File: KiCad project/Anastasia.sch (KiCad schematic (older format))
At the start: 0 parts

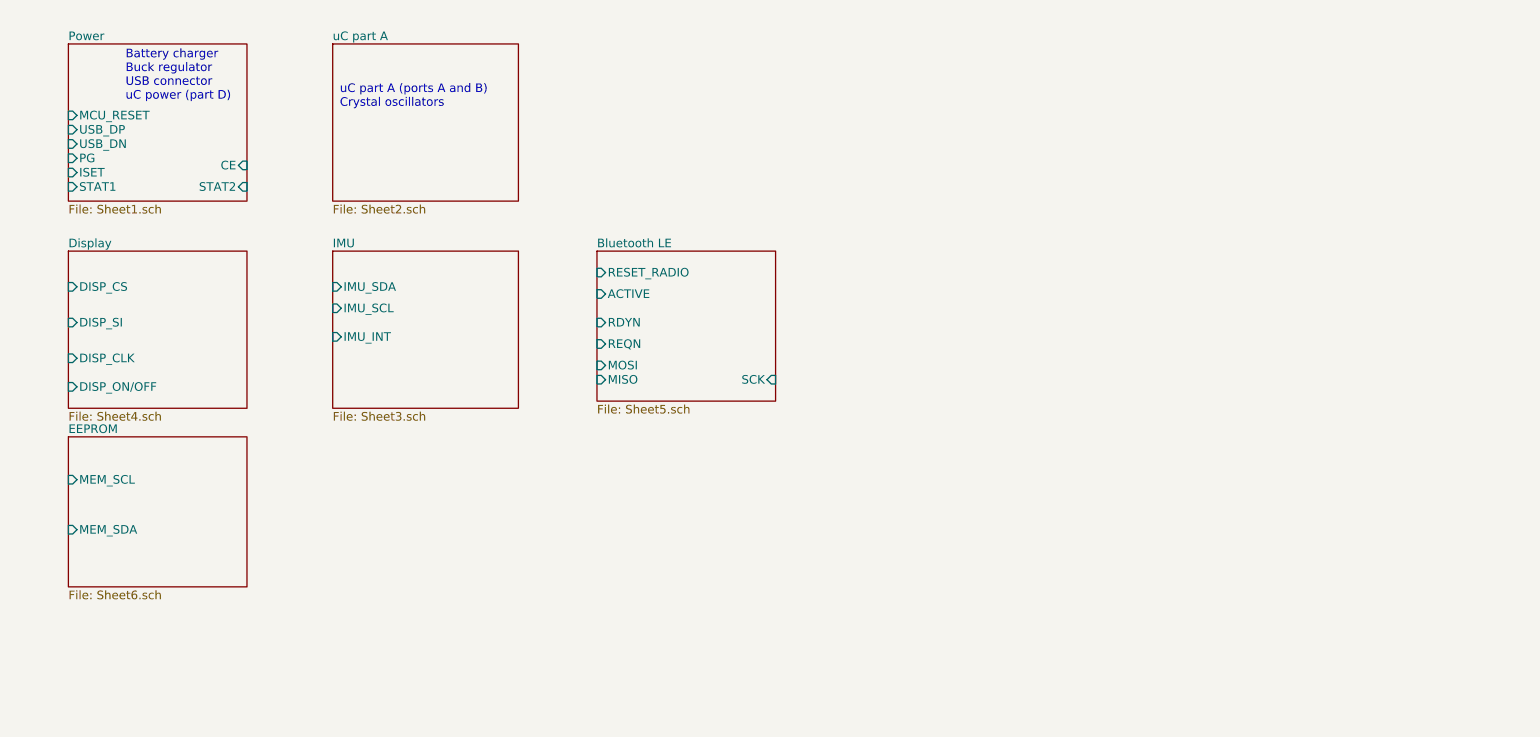
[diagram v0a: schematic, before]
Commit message: IC packages, bugfixes
drawings for IC packages, associations, schematic fixes
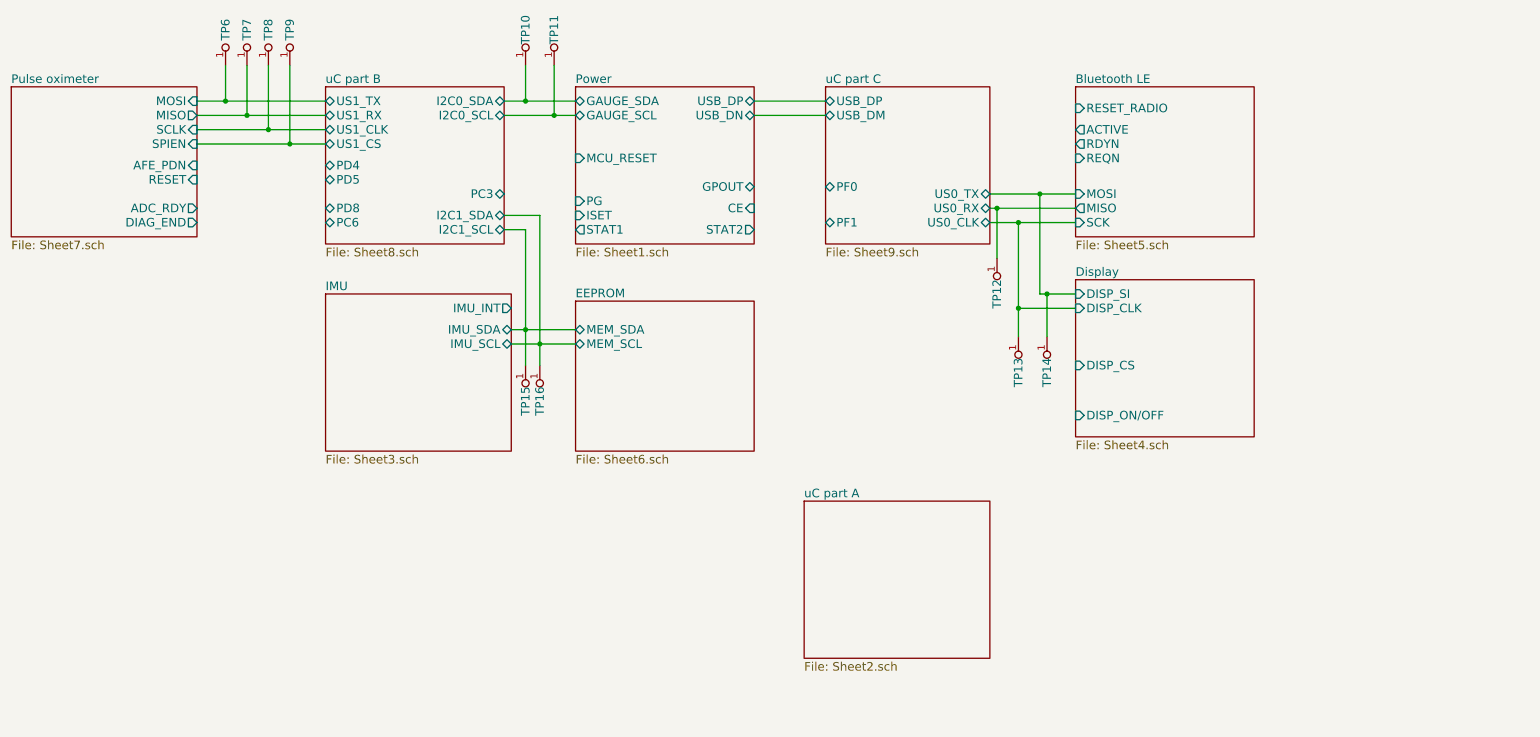
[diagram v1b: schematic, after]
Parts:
- added TP10, TP11, TP12, TP13, TP14, TP15, TP16, TP6, TP7, TP8, TP9: TESTPAD, symbol TESTPAD
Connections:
- net Bluetooth LE/MISO: now also TP12.1
- net Bluetooth LE/MOSI: now also TP14.1
- net Bluetooth LE/SCK: now also TP13.1
- net EEPROM/MEM_SCL: now also TP16.1
- net EEPROM/MEM_SDA: now also TP15.1
- new net Power/GAUGE_SCL: TP11.1
- new net Power/GAUGE_SDA: TP10.1
- new net Pulse oximeter /MISO: TP7.1
- new net Pulse oximeter /MOSI: TP6.1
- new net Pulse oximeter /SCLK: TP8.1
- new net Pulse oximeter /SPIEN: TP9.1
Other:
- note removed: "Battery charger\nBuck regulator\nUSB connector\nuC power (part D)"
- note removed: "uC part A (ports A and B)\nCrystal oscillators\n"

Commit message: New packages, PCB
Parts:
- TP1: renamed from TP6; footprint (none) -> Measurement_Points:Measurement_Point_Round-SMD-Pad_Small
- TP10: renamed from TP15; footprint (none) -> Measurement_Points:Measurement_Point_Round-SMD-Pad_Small
- TP11: renamed from TP16; footprint (none) -> Measurement_Points:Measurement_Point_Round-SMD-Pad_Small
- TP2: renamed from TP7; footprint (none) -> Measurement_Points:Measurement_Point_Round-SMD-Pad_Small
- TP3: renamed from TP8; footprint (none) -> Measurement_Points:Measurement_Point_Round-SMD-Pad_Small
- TP4: renamed from TP9; footprint (none) -> Measurement_Points:Measurement_Point_Round-SMD-Pad_Small
- TP5: renamed from TP10; footprint (none) -> Measurement_Points:Measurement_Point_Round-SMD-Pad_Small
- TP6: renamed from TP11; footprint (none) -> Measurement_Points:Measurement_Point_Round-SMD-Pad_Small
- TP7: renamed from TP12; footprint (none) -> Measurement_Points:Measurement_Point_Round-SMD-Pad_Small
- TP8: renamed from TP13; footprint (none) -> Measurement_Points:Measurement_Point_Round-SMD-Pad_Small
- TP9: renamed from TP14; footprint (none) -> Measurement_Points:Measurement_Point_Round-SMD-Pad_Small
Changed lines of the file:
@@
 Connection ~ 4400 2950
 $Comp
-L TESTPAD TP6
+L TESTPAD TP1
 U 1 1 550D1F0B
 P 2200 1000
-F 0 "TP6" H 2450 1000 60  0000 C CNN
+F 0 "TP1" H 2450 1000 60  0000 C CNN
 F 1 "TESTPAD" H 2250 800 60  0001 C CNN
-F 2 "" H 2450 1000 60  0000 C CNN
+F 2 "Measurement_Points:Measurement_Point_Round-SMD-Pad_Small" H 2450 1000 60  0001 C CNN
 F 3 "" H 2450 1000 60  0000 C CNN
 	1    2200 1000
@@
 $EndComp
 $Comp
-L TESTPAD TP7
+L TESTPAD TP2
 U 1 1 550D1F40
 P 2350 1000
-F 0 "TP7" H 2600 1000 60  0000 C CNN
+F 0 "TP2" H 2600 1000 60  0000 C CNN
 F 1 "TESTPAD" H 2400 800 60  0001 C CNN
-F 2 "" H 2600 1000 60  0000 C CNN
+F 2 "Measurement_Points:Measurement_Point_Round-SMD-Pad_Small" H 2600 1000 60  0001 C CNN
 F 3 "" H 2600 1000 60  0000 C CNN
 	1    2350 1000
@@
 $EndComp
 $Comp
-L TESTPAD TP8
+L TESTPAD TP3
 U 1 1 550D1F5F
 P 2500 1000
-F 0 "TP8" H 2750 1000 60  0000 C CNN
+F 0 "TP3" H 2750 1000 60  0000 C CNN
 F 1 "TESTPAD" H 2550 800 60  0001 C CNN
-F 2 "" H 2750 1000 60  0000 C CNN
+F 2 "Measurement_Points:Measurement_Point_Round-SMD-Pad_Small" H 2750 1000 60  0001 C CNN
 F 3 "" H 2750 1000 60  0000 C CNN
 	1    2500 1000
@@
 $EndComp
 $Comp
-L TESTPAD TP9
+L TESTPAD TP4
 U 1 1 550D1F7E
 P 2650 1000
-F 0 "TP9" H 2900 1000 60  0000 C CNN
+F 0 "TP4" H 2900 1000 60  0000 C CNN
 F 1 "TESTPAD" H 2700 800 60  0001 C CNN
-F 2 "" H 2900 1000 60  0000 C CNN
+F 2 "Measurement_Points:Measurement_Point_Round-SMD-Pad_Small" H 2900 1000 60  0001 C CNN
 F 3 "" H 2900 1000 60  0000 C CNN
 	1    2650 1000
@@
 Connection ~ 2650 1550
 $Comp
-L TESTPAD TP10
+L TESTPAD TP5
 U 1 1 550D353F
 P 4300 1000
-F 0 "TP10" H 4550 1000 60  0000 C CNN
+F 0 "TP5" H 4550 1000 60  0000 C CNN
 F 1 "TESTPAD" H 4350 800 60  0001 C CNN
-F 2 "" H 4550 1000 60  0000 C CNN
+F 2 "Measurement_Points:Measurement_Point_Round-SMD-Pad_Small" H 4550 1000 60  0001 C CNN
 F 3 "" H 4550 1000 60  0000 C CNN
 	1    4300 1000
@@
 $EndComp
 $Comp
-L TESTPAD TP11
+L TESTPAD TP6
 U 1 1 550D3564
 P 4500 1000
-F 0 "TP11" H 4750 1000 60  0000 C CNN
+F 0 "TP6" H 4750 1000 60  0000 C CNN
 F 1 "TESTPAD" H 4550 800 60  0001 C CNN
-F 2 "" H 4750 1000 60  0000 C CNN
+F 2 "Measurement_Points:Measurement_Point_Round-SMD-Pad_Small" H 4750 1000 60  0001 C CNN
 F 3 "" H 4750 1000 60  0000 C CNN
 	1    4500 1000
@@
 $EndComp
 $Comp
-L TESTPAD TP15
+L TESTPAD TP10
 U 1 1 550D3583
 P 4300 3100
-F 0 "TP15" H 4550 3100 60  0000 C CNN
+F 0 "TP10" H 4550 3100 60  0000 C CNN
 F 1 "TESTPAD" H 4350 2900 60  0001 C CNN
-F 2 "" H 4550 3100 60  0000 C CNN
+F 2 "Measurement_Points:Measurement_Point_Round-SMD-Pad_Small" H 4550 3100 60  0001 C CNN
 F 3 "" H 4550 3100 60  0000 C CNN
 	1    4300 3100
@@
 $EndComp
 $Comp
-L TESTPAD TP16
+L TESTPAD TP11
 U 1 1 550D359E
 P 4400 3100
-F 0 "TP16" H 4650 3100 60  0000 C CNN
+F 0 "TP11" H 4650 3100 60  0000 C CNN
 F 1 "TESTPAD" H 4450 2900 60  0001 C CNN
-F 2 "" H 4650 3100 60  0000 C CNN
+F 2 "Measurement_Points:Measurement_Point_Round-SMD-Pad_Small" H 4650 3100 60  0001 C CNN
 F 3 "" H 4650 3100 60  0000 C CNN
 	1    4400 3100
@@
 Connection ~ 4500 1350
 $Comp
-L TESTPAD TP13
+L TESTPAD TP8
 U 1 1 550D3905
 P 7750 2900
-F 0 "TP13" H 8000 2900 60  0000 C CNN
+F 0 "TP8" H 8000 2900 60  0000 C CNN
 F 1 "TESTPAD" H 7800 2700 60  0001 C CNN
-F 2 "" H 8000 2900 60  0000 C CNN
+F 2 "Measurement_Points:Measurement_Point_Round-SMD-Pad_Small" H 8000 2900 60  0001 C CNN
 F 3 "" H 8000 2900 60  0000 C CNN
 	1    7750 2900
@@
 $EndComp
 $Comp
-L TESTPAD TP14
+L TESTPAD TP9
 U 1 1 550D3920
 P 7950 2900
-F 0 "TP14" H 8200 2900 60  0000 C CNN
+F 0 "TP9" H 8200 2900 60  0000 C CNN
 F 1 "TESTPAD" H 8000 2700 60  0001 C CNN
-F 2 "" H 8200 2900 60  0000 C CNN
+F 2 "Measurement_Points:Measurement_Point_Round-SMD-Pad_Small" H 8200 2900 60  0001 C CNN
 F 3 "" H 8200 2900 60  0000 C CNN
 	1    7950 2900
@@
 Connection ~ 7950 2600
 $Comp
-L TESTPAD TP12
+L TESTPAD TP7
 U 1 1 550D3AEA
 P 7600 2350
-F 0 "TP12" H 7850 2350 60  0000 C CNN
+F 0 "TP7" H 7850 2350 60  0000 C CNN
 F 1 "TESTPAD" H 7650 2150 60  0001 C CNN
-F 2 "" H 7850 2350 60  0000 C CNN
+F 2 "Measurement_Points:Measurement_Point_Round-SMD-Pad_Small" H 7850 2350 60  0001 C CNN
 F 3 "" H 7850 2350 60  0000 C CNN
 	1    7600 2350

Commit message: Schematics, PCB design
New schematics for the pulse oximeter, PCB layout design
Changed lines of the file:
@@
 $EndSheet
 $Sheet
-S 6250 4050 1300 1100
+S 2900 3900 1300 1100
 U 5504D17E
 F0 "uC part A" 60
 F1 "Sheet2.sch" 60
+F2 "PA8" I L 2900 4100 60
 $EndSheet
 $Sheet
@@
 F2 "IMU_SDA" B R 4200 2850 60
 F3 "IMU_SCL" B R 4200 2950 60
-F4 "IMU_INT" O R 4200 2700 60
+F4 "IMU_INT" O L 2900 3550 60
 $EndSheet
 $Sheet
@@
 	7600 2350 7600 2000
 Connection ~ 7600 2000
+Wire Wire Line
+	2900 4100 2650 4100
+Wire Wire Line
+	2650 4100 2650 3550
+Wire Wire Line
+	2650 3550 2900 3550
 $EndSCHEMATC

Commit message: PCB design
Routing for the main components, except for the power section
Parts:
- TP1, TP10, TP11, TP2, TP3, TP4, TP5, TP6, TP7, TP8, TP9: footprint Measurement_Points:Measurement_Point_Round-SMD-Pad_Small -> Anastasia:Test_Point_Round-SMD-Pad
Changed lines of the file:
@@
 F1 "Sheet2.sch" 60
 F2 "PA8" I L 2900 4100 60
+F3 "PA0" T R 4200 4100 60
 $EndSheet
 $Sheet
@@
 F5 "SPIEN" I R 2000 1550 60
 F6 "RESET" I R 2000 1800 60
-F7 "ADC_RDY" O R 2000 2000 60
-F8 "AFE_PDN" I R 2000 1700 60
+F7 "ADC_RDY" O R 2000 1700 60
+F8 "AFE_PDN" I R 2000 2000 60
 F9 "DIAG_END" O R 2000 2100 60
 $EndSheet
@@
 F11 "PD5" T L 2900 1800 60
 F12 "PC3" T R 4150 1900 60
-F13 "PD8" T L 2900 2000 60
-F14 "PC6" T L 2900 2100 60
+F13 "PD8" T R 4150 1600 60
+F14 "PC6" T R 4150 1750 60
+F15 "PD6" B L 2900 2100 60
+F16 "PD7" B L 2900 2000 60
 $EndSheet
 $Sheet
@@
 F5 "US0_RX" T R 7550 2000 60
 F6 "US0_CLK" T R 7550 2100 60
-F7 "PF0" T L 6400 1850 60
-F8 "PF1" T L 6400 2100 60
+F7 "PF0" T R 7550 1300 60
+F8 "PF1" T R 7550 1550 60
+F9 "PF2" T R 7550 1650 60
 $EndSheet
 $Sheet
@@
 F 0 "TP1" H 2450 1000 60  0000 C CNN
 F 1 "TESTPAD" H 2250 800 60  0001 C CNN
-F 2 "Measurement_Points:Measurement_Point_Round-SMD-Pad_Small" H 2450 1000 60  0001 C CNN
+F 2 "Anastasia:Test_Point_Round-SMD-Pad" H 2450 1000 60  0001 C CNN
 F 3 "" H 2450 1000 60  0000 C CNN
 	1    2200 1000
@@
 F 0 "TP2" H 2600 1000 60  0000 C CNN
 F 1 "TESTPAD" H 2400 800 60  0001 C CNN
-F 2 "Measurement_Points:Measurement_Point_Round-SMD-Pad_Small" H 2600 1000 60  0001 C CNN
+F 2 "Anastasia:Test_Point_Round-SMD-Pad" H 2600 1000 60  0001 C CNN
 F 3 "" H 2600 1000 60  0000 C CNN
 	1    2350 1000
@@
 F 0 "TP3" H 2750 1000 60  0000 C CNN
 F 1 "TESTPAD" H 2550 800 60  0001 C CNN
-F 2 "Measurement_Points:Measurement_Point_Round-SMD-Pad_Small" H 2750 1000 60  0001 C CNN
+F 2 "Anastasia:Test_Point_Round-SMD-Pad" H 2750 1000 60  0001 C CNN
 F 3 "" H 2750 1000 60  0000 C CNN
 	1    2500 1000
@@
 F 0 "TP4" H 2900 1000 60  0000 C CNN
 F 1 "TESTPAD" H 2700 800 60  0001 C CNN
-F 2 "Measurement_Points:Measurement_Point_Round-SMD-Pad_Small" H 2900 1000 60  0001 C CNN
+F 2 "Anastasia:Test_Point_Round-SMD-Pad" H 2900 1000 60  0001 C CNN
 F 3 "" H 2900 1000 60  0000 C CNN
 	1    2650 1000
@@
 F 0 "TP5" H 4550 1000 60  0000 C CNN
 F 1 "TESTPAD" H 4350 800 60  0001 C CNN
-F 2 "Measurement_Points:Measurement_Point_Round-SMD-Pad_Small" H 4550 1000 60  0001 C CNN
+F 2 "Anastasia:Test_Point_Round-SMD-Pad" H 4550 1000 60  0001 C CNN
 F 3 "" H 4550 1000 60  0000 C CNN
 	1    4300 1000
@@
 F 0 "TP6" H 4750 1000 60  0000 C CNN
 F 1 "TESTPAD" H 4550 800 60  0001 C CNN
-F 2 "Measurement_Points:Measurement_Point_Round-SMD-Pad_Small" H 4750 1000 60  0001 C CNN
+F 2 "Anastasia:Test_Point_Round-SMD-Pad" H 4750 1000 60  0001 C CNN
 F 3 "" H 4750 1000 60  0000 C CNN
 	1    4500 1000
@@
 F 0 "TP10" H 4550 3100 60  0000 C CNN
 F 1 "TESTPAD" H 4350 2900 60  0001 C CNN
-F 2 "Measurement_Points:Measurement_Point_Round-SMD-Pad_Small" H 4550 3100 60  0001 C CNN
+F 2 "Anastasia:Test_Point_Round-SMD-Pad" H 4550 3100 60  0001 C CNN
 F 3 "" H 4550 3100 60  0000 C CNN
 	1    4300 3100
@@
 F 0 "TP11" H 4650 3100 60  0000 C CNN
 F 1 "TESTPAD" H 4450 2900 60  0001 C CNN
-F 2 "Measurement_Points:Measurement_Point_Round-SMD-Pad_Small" H 4650 3100 60  0001 C CNN
+F 2 "Anastasia:Test_Point_Round-SMD-Pad" H 4650 3100 60  0001 C CNN
 F 3 "" H 4650 3100 60  0000 C CNN
 	1    4400 3100
@@
 F 0 "TP8" H 8000 2900 60  0000 C CNN
 F 1 "TESTPAD" H 7800 2700 60  0001 C CNN
-F 2 "Measurement_Points:Measurement_Point_Round-SMD-Pad_Small" H 8000 2900 60  0001 C CNN
+F 2 "Anastasia:Test_Point_Round-SMD-Pad" H 8000 2900 60  0001 C CNN
 F 3 "" H 8000 2900 60  0000 C CNN
 	1    7750 2900
@@
 F 0 "TP9" H 8200 2900 60  0000 C CNN
 F 1 "TESTPAD" H 8000 2700 60  0001 C CNN
-F 2 "Measurement_Points:Measurement_Point_Round-SMD-Pad_Small" H 8200 2900 60  0001 C CNN
+F 2 "Anastasia:Test_Point_Round-SMD-Pad" H 8200 2900 60  0001 C CNN
 F 3 "" H 8200 2900 60  0000 C CNN
 	1    7950 2900
@@
 F 0 "TP7" H 7850 2350 60  0000 C CNN
 F 1 "TESTPAD" H 7650 2150 60  0001 C CNN
-F 2 "Measurement_Points:Measurement_Point_Round-SMD-Pad_Small" H 7850 2350 60  0001 C CNN
+F 2 "Anastasia:Test_Point_Round-SMD-Pad" H 7850 2350 60  0001 C CNN
 F 3 "" H 7850 2350 60  0000 C CNN
 	1    7600 2350
@@
 Wire Wire Line
 	2650 3550 2900 3550
+Wire Wire Line
+	8150 1650 7550 1650
+Wire Wire Line
+	8150 1450 7950 1450
+Wire Wire Line
+	7950 1450 7950 850
+Wire Wire Line
+	7950 850  9700 850
+Wire Wire Line
+	9700 850  9700 4100
+Wire Wire Line
+	9700 4100 4200 4100
+Wire Wire Line
+	8150 1300 7550 1300
+Wire Wire Line
+	7550 1550 8150 1550
+Connection ~ 5100 1450
+Wire Wire Line
+	2900 1700 2000 1700
+Wire Wire Line
+	2000 1800 2900 1800
+Wire Wire Line
+	2000 2000 2900 2000
+Wire Wire Line
+	2000 2100 2900 2100
 $EndSCHEMATC

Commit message: PCB finalised, Gerbers created for v0.5
New footprints, fixes in schematic, PCB final design, plotted Gerbers
for prototype production
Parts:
- removed TP1, TP10, TP2, TP3, TP4, TP5, TP6, TP8, TP9: TESTPAD, Anastasia:Test_Point_Round-SMD-Pad, symbol TESTPAD
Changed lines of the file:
@@
 $EndDescr
-$Sheet
-S 4650 1150 1250 1100
-U 55046F13
-F0 "Power" 60
-F1 "Sheet1.sch" 60
-F2 "MCU_RESET" I L 4650 1650 60
-F3 "USB_DP" T R 5900 1250 60
-F4 "USB_DN" T R 5900 1350 60
-F5 "PG" I L 4650 1950 60
-F6 "ISET" I L 4650 2050 60
-F7 "STAT1" O L 4650 2150 60
-F8 "STAT2" O R 5900 2150 60
-F9 "CE" I R 5900 2000 60
-F10 "GPOUT" B R 5900 1850 60
-F11 "GAUGE_SCL" B L 4650 1350 60
-F12 "GAUGE_SDA" B L 4650 1250 60
-$EndSheet
 $Sheet
 S 2900 3900 1300 1100
@@
 F2 "PA8" I L 2900 4100 60
 F3 "PA0" T R 4200 4100 60
+F4 "PA1" T R 4200 4250 60
+F5 "PA2" T R 4200 4400 60
+F6 "PA9" T R 4200 4850 60
+F7 "PA10" T R 4200 4700 60
 $EndSheet
 $Sheet
@@
 F0 "Display" 60
 F1 "Sheet4.sch" 60
-F2 "DISP_CS" I L 8150 3100 60
+F2 "DISP_CS" I L 8150 3300 60
 F3 "DISP_SI" I L 8150 2600 60
 F4 "DISP_CLK" I L 8150 2700 60
@@
 F8 "PF1" T R 7550 1550 60
 F9 "PF2" T R 7550 1650 60
+F10 "PE9" T L 6400 2150 60
+F11 "PE8" T L 6400 2000 60
 $EndSheet
 $Sheet
@@
 	4150 1250 4650 1250
 Wire Wire Line
-	4650 1350 4150 1350
+	4150 1350 4650 1350
 Wire Wire Line
 	2000 1250 2900 1250
@@
 Connection ~ 7900 1900
 Wire Wire Line
-	7750 2100 7750 2900
-Wire Wire Line
 	7750 2700 8150 2700
 Connection ~ 7750 2100
@@
 	4200 2950 4650 2950
 Wire Wire Line
-	4150 2150 4300 2150
-Wire Wire Line
-	4300 2150 4300 3100
-Connection ~ 4300 2850
-Wire Wire Line
-	4150 2050 4400 2050
-Wire Wire Line
-	4400 2050 4400 3100
+	4400 2950 4400 3100
 Connection ~ 4400 2950
-$Comp
-L TESTPAD TP1
-U 1 1 550D1F0B
-P 2200 1000
-F 0 "TP1" H 2450 1000 60  0000 C CNN
-F 1 "TESTPAD" H 2250 800 60  0001 C CNN
-F 2 "Anastasia:Test_Point_Round-SMD-Pad" H 2450 1000 60  0001 C CNN
-F 3 "" H 2450 1000 60  0000 C CNN
-	1    2200 1000
-	0    -1   -1   0
-$EndComp
-$Comp
-L TESTPAD TP2
-U 1 1 550D1F40
-P 2350 1000
-F 0 "TP2" H 2600 1000 60  0000 C CNN
-F 1 "TESTPAD" H 2400 800 60  0001 C CNN
-F 2 "Anastasia:Test_Point_Round-SMD-Pad" H 2600 1000 60  0001 C CNN
-F 3 "" H 2600 1000 60  0000 C CNN
-	1    2350 1000
-	0    -1   -1   0
-$EndComp
-$Comp
-L TESTPAD TP3
-U 1 1 550D1F5F
-P 2500 1000
-F 0 "TP3" H 2750 1000 60  0000 C CNN
-F 1 "TESTPAD" H 2550 800 60  0001 C CNN
-F 2 "Anastasia:Test_Point_Round-SMD-Pad" H 2750 1000 60  0001 C CNN
-F 3 "" H 2750 1000 60  0000 C CNN
-	1    2500 1000
-	0    -1   -1   0
-$EndComp
-$Comp
-L TESTPAD TP4
-U 1 1 550D1F7E
-P 2650 1000
-F 0 "TP4" H 2900 1000 60  0000 C CNN
-F 1 "TESTPAD" H 2700 800 60  0001 C CNN
-F 2 "Anastasia:Test_Point_Round-SMD-Pad" H 2900 1000 60  0001 C CNN
-F 3 "" H 2900 1000 60  0000 C CNN
-	1    2650 1000
-	0    -1   -1   0
-$EndComp
-Wire Wire Line
-	2200 1000 2200 1250
-Connection ~ 2200 1250
-Wire Wire Line
-	2350 1000 2350 1350
-Connection ~ 2350 1350
-Wire Wire Line
-	2500 1000 2500 1450
-Connection ~ 2500 1450
-Wire Wire Line
-	2650 1000 2650 1550
-Connection ~ 2650 1550
-$Comp
-L TESTPAD TP5
-U 1 1 550D353F
-P 4300 1000
-F 0 "TP5" H 4550 1000 60  0000 C CNN
-F 1 "TESTPAD" H 4350 800 60  0001 C CNN
-F 2 "Anastasia:Test_Point_Round-SMD-Pad" H 4550 1000 60  0001 C CNN
-F 3 "" H 4550 1000 60  0000 C CNN
-	1    4300 1000
-	0    -1   -1   0
-$EndComp
-$Comp
-L TESTPAD TP6
-U 1 1 550D3564
-P 4500 1000
-F 0 "TP6" H 4750 1000 60  0000 C CNN
-F 1 "TESTPAD" H 4550 800 60  0001 C CNN
-F 2 "Anastasia:Test_Point_Round-SMD-Pad" H 4750 1000 60  0001 C CNN
-F 3 "" H 4750 1000 60  0000 C CNN
-	1    4500 1000
-	0    -1   -1   0
-$EndComp
-$Comp
-L TESTPAD TP10
-U 1 1 550D3583
-P 4300 3100
-F 0 "TP10" H 4550 3100 60  0000 C CNN
-F 1 "TESTPAD" H 4350 2900 60  0001 C CNN
-F 2 "Anastasia:Test_Point_Round-SMD-Pad" H 4550 3100 60  0001 C CNN
-F 3 "" H 4550 3100 60  0000 C CNN
-	1    4300 3100
-	0    1    1    0
-$EndComp
 $Comp
 L TESTPAD TP11
@@
 	0    1    1    0
 $EndComp
-Wire Wire Line
-	4300 1000 4300 1250
-Connection ~ 4300 1250
-Wire Wire Line
-	4500 1000 4500 1350
-Connection ~ 4500 1350
-$Comp
-L TESTPAD TP8
-U 1 1 550D3905
-P 7750 2900
-F 0 "TP8" H 8000 2900 60  0000 C CNN
-F 1 "TESTPAD" H 7800 2700 60  0001 C CNN
-F 2 "Anastasia:Test_Point_Round-SMD-Pad" H 8000 2900 60  0001 C CNN
-F 3 "" H 8000 2900 60  0000 C CNN
-	1    7750 2900
-	0    1    1    0
-$EndComp
-$Comp
-L TESTPAD TP9
-U 1 1 550D3920
-P 7950 2900
-F 0 "TP9" H 8200 2900 60  0000 C CNN
-F 1 "TESTPAD" H 8000 2700 60  0001 C CNN
-F 2 "Anastasia:Test_Point_Round-SMD-Pad" H 8200 2900 60  0001 C CNN
-F 3 "" H 8200 2900 60  0000 C CNN
-	1    7950 2900
-	0    1    1    0
-$EndComp
-Connection ~ 7750 2700
-Wire Wire Line
-	7950 2900 7950 2600
-Connection ~ 7950 2600
 $Comp
 L TESTPAD TP7
@@
 Wire Wire Line
 	7550 1550 8150 1550
-Connection ~ 5100 1450
 Wire Wire Line
 	2900 1700 2000 1700
@@
 Wire Wire Line
 	2000 2100 2900 2100
+$Sheet
+S 4650 1150 1250 1100
+U 55046F13
+F0 "Power" 60
+F1 "Sheet1.sch" 60
+F2 "MCU_RESET" I L 4650 1850 60
+F3 "USB_DP" T R 5900 1250 60
+F4 "USB_DN" T R 5900 1350 60
+F5 "PG" I L 4650 1950 60
+F6 "ISET" I L 4650 2050 60
+F7 "STAT1" O R 5900 1850 60
+F8 "STAT2" O R 5900 2150 60
+F9 "CE" I L 4650 2150 60
+F10 "GPOUT" B L 4650 1600 60
+F11 "GAUGE_SCL" B L 4650 1350 60
+F12 "GAUGE_SDA" B L 4650 1250 60
+$EndSheet
+Wire Wire Line
+	4650 1600 4150 1600
+Wire Wire Line
+	8150 3300 6350 3300
+Wire Wire Line
+	6350 3300 6350 2150
+Wire Wire Line
+	6350 2150 6400 2150
+Wire Wire Line
+	6400 2000 6150 2000
+Wire Wire Line
+	6150 2000 6150 3450
+Wire Wire Line
+	6150 3450 8150 3450
+Wire Wire Line
+	4200 4250 4450 4250
+Wire Wire Line
+	4450 4250 4450 2050
+Wire Wire Line
+	4450 2050 4650 2050
+Wire Wire Line
+	4200 4400 4550 4400
+Wire Wire Line
+	4550 4400 4550 2150
+Wire Wire Line
+	4550 2150 4650 2150
+Wire Wire Line
+	5900 2150 6000 2150
+Wire Wire Line
+	6000 2150 6000 4700
+Wire Wire Line
+	6000 4700 4200 4700
+Wire Wire Line
+	4200 4850 6050 4850
+Wire Wire Line
+	6050 4850 6050 1850
+Wire Wire Line
+	6050 1850 5900 1850
+Wire Wire Line
+	7750 2100 7750 2700
+Wire Wire Line
+	4150 2150 4250 2150
+Wire Wire Line
+	4250 2150 4250 2950
+Connection ~ 4250 2950
+Wire Wire Line
+	4150 2050 4350 2050
+Wire Wire Line
+	4350 2050 4350 2850
+Connection ~ 4350 2850
 $EndSCHEMATC
